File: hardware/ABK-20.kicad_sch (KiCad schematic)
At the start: 46 parts, among them J1 CONN_01X04, J2 CONN_01X04, J3 CONN_02X03, J4 Con_3-5V, J5 USB_OTG, J6 Sync_Jumper, SW1 SW_Push, SW2 SW_Push, SW3 SW_SPDT_MSM, SW4 SW_Push, U1 ATTINY85-20SU, U2 PAM8002, U3 7805

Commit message: Optimize PAM8002 audio amplifier circuit: set R14=22k for unity gain, C5=1uF, and add C8 100nF decoupling
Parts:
- added C8: 100nF, 8Bitmixtape_reworked:C_1206_HandSoldering, symbol ABK-20-rescue1:C
- C5: value 10uF -> 1uF
- R14: value 330 -> 22k
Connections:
- net GND: now also C8.2
- net VCC: now also C8.1
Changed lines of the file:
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@@
 			)
 		)
-		(property "Value" "330"
+		(property "Value" "22k"
 			(at 154.94 39.37 90)
 			(effects
@@
 			)
 		)
-		(property "Value" "10uF"
+		(property "Value" "1uF"
 			(at 137.16 40.005 0)
 			(effects
@@
 	)
 	(embedded_fonts no)
+	(junction
+		(at 107.95 24.13)
+		(diameter 0)
+		(color 0 0 0 0)
+	)
+	(junction
+		(at 107.95 36.83)
+		(diameter 0)
+		(color 0 0 0 0)
+	)
+	(wire
+		(pts
+			(xy 107.95 24.13) (xy 116.84 24.13)
+		)
+		(stroke
+			(width 0)
+			(type default)
+		)
+	)
+	(wire
+		(pts
+			(xy 116.84 24.13) (xy 116.84 26.67)
+		)
+		(stroke
+			(width 0)
+			(type default)
+		)
+	)
+	(wire
+		(pts
+			(xy 116.84 34.29) (xy 116.84 36.83)
+		)
+		(stroke
+			(width 0)
+			(type default)
+		)
+	)
+	(wire
+		(pts
+			(xy 116.84 36.83) (xy 107.95 36.83)
+		)
+		(stroke
+			(width 0)
+			(type default)
+		)
+	)
+	(symbol
+		(lib_name "C_11")
+		(lib_id "ABK-20-rescue1:C")
+		(at 116.84 30.48 0)
+		(unit 1)
+		(exclude_from_sim no)
+		(in_bom yes)
+		(on_board yes)
+		(dnp no)
+		(property "Reference" "C8"
+			(at 117.475 27.94 0)
+			(effects
+				(font
+					(size 1.27 1.27)
+				)
+				(justify left)
+			)
+		)
+		(property "Value" "100nF"
+			(at 117.475 33.02 0)
+			(effects
+				(font
+					(size 1.27 1.27)
+				)
+				(justify left)
+			)
+		)
+		(property "Footprint" "8Bitmixtape_reworked:C_1206_HandSoldering"
+			(at 117.8052 34.29 0)
+			(effects
+				(font
+					(size 1.27 1.27)
+				)
+				(hide yes)
+			)
+		)
+		(property "Datasheet" ""
+			(at 116.84 30.48 0)
+			(effects
+				(font
+					(size 1.27 1.27)
+				)
+				(hide yes)
+			)
+		)
+		(property "Description" ""
+			(at 116.84 30.48 0)
+			(effects
+				(font
+					(size 1.27 1.27)
+				)
+			)
+		)
+		(pin "1"
+		)
+		(pin "2"
+		)
+		(instances
+			(project "ABK-20"
+				(path "/586acb5e-8acc-4ed8-b81f-7b15963d193b"
+					(reference "C8")
+					(unit 1)
+				)
+			)
+		)
+	)
 )

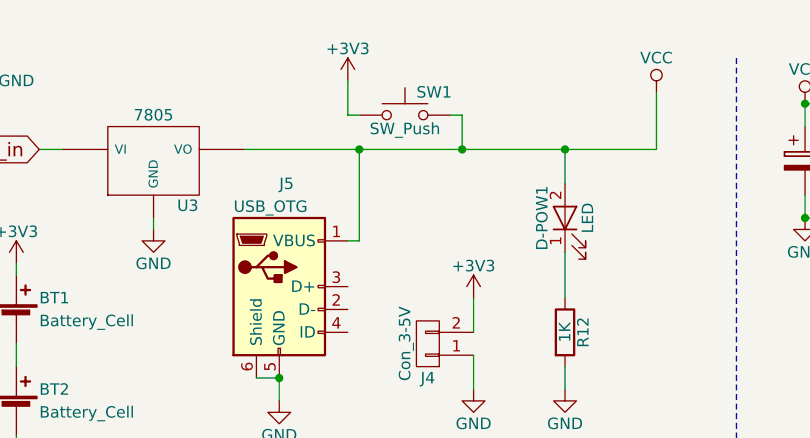
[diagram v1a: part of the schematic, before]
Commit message: Implement diode OR-ing power architecture with Schottky isolation and master latching switch
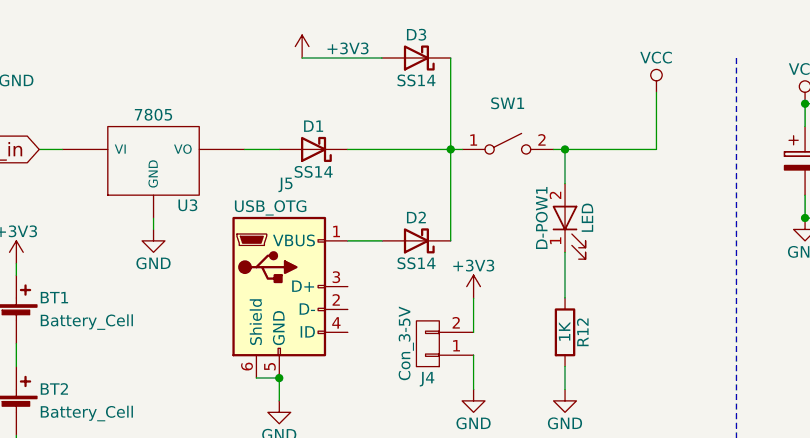
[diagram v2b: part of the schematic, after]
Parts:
- removed SW1: SW_Push, 8Bitmixtape_reworked:Push_SWITCH_hole, symbol mixtape_schematics:SW_Push
- added D1, D2, D3: SS14, Diode_SMD:D_SMA, symbol mixtape_schematics:D_Schottky
- added SW1: SW_SPST, 8Bitmixtape_reworked:Push_SWITCH_hole, symbol mixtape_schematics:SW_SPST
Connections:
- net +3V3: now also D3.2 (A)
- net VCC: now also SW1.2 (B); no longer J5.1 (VBUS), U3.VO
- new net: D1.2 (A), U3.VO
- new net: D2.2 (A), J5.1 (VBUS)
- new net: D1.1 (K), D2.1 (K), D3.1 (K), SW1.1 (A)
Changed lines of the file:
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@@
 		(color 0 0 0 0)
 	)
-	(junction
-		(at 58.42 29.21)
-		(diameter 0)
-		(color 0 0 0 0)
-	)
-	(junction
+		(junction
 		(at 140.97 111.76)
 		(diameter 0)
@@
 		(color 0 0 0 0)
 	)
-	(junction
-		(at 69.85 29.21)
-		(diameter 0)
-		(color 0 0 0 0)
-	)
-	(wire
+		(wire
 		(pts
 			(xy 248.92 152.4) (xy 242.57 152.4)
@@
 		)
 	)
-	(wire
-		(pts
-			(xy 45.72 29.21) (xy 58.42 29.21)
-		)
-		(stroke
-			(width 0)
-			(type default)
-		)
-	)
-	(wire
+		(wire
 		(pts
 			(xy 217.17 129.54) (xy 222.25 129.54)
@@
 		)
 	)
-	(wire
-		(pts
-			(xy 58.42 39.37) (xy 58.42 29.21)
-		)
-		(stroke
-			(width 0)
-			(type default)
-		)
-	)
-	(wire
+		(wire
 		(pts
 			(xy 199.39 92.71) (xy 248.92 92.71)
@@
 		)
 	)
-	(wire
-		(pts
-			(xy 57.15 25.4) (xy 58.42 25.4)
-		)
-		(stroke
-			(width 0)
-			(type default)
-		)
-	)
-	(wire
+		(wire
 		(pts
 			(xy 246.38 157.48) (xy 246.38 160.02)
@@
 		)
 	)
-	(wire
-		(pts
-			(xy 69.85 29.21) (xy 81.28 29.21)
-		)
-		(stroke
-			(width 0)
-			(type default)
-		)
-	)
-	(wire
+		(wire
 		(pts
 			(xy 161.29 39.37) (xy 165.1 39.37)
@@
 		)
 	)
-	(wire
-		(pts
-			(xy 58.42 29.21) (xy 69.85 29.21)
-		)
-		(stroke
-			(width 0)
-			(type default)
-		)
-	)
-	(wire
+		(wire
 		(pts
 			(xy 71.12 137.16) (xy 71.12 142.24)
@@
 		)
 	)
-	(wire
-		(pts
-			(xy 69.85 25.4) (xy 69.85 29.21)
-		)
-		(stroke
-			(width 0)
-			(type default)
-		)
-	)
-	(wire
+		(wire
 		(pts
 			(xy 177.8 24.13) (xy 177.8 34.29)
@@
 		)
 	)
-	(wire
-		(pts
-			(xy 57.15 21.59) (xy 57.15 25.4)
-		)
-		(stroke
-			(width 0)
-			(type default)
-		)
-	)
-	(wire
+		(wire
 		(pts
 			(xy 71.12 52.07) (xy 71.12 55.88)
@@
 		)
 	)
-	(wire
-		(pts
-			(xy 57.15 39.37) (xy 58.42 39.37)
-		)
-		(stroke
-			(width 0)
-			(type default)
-		)
-	)
-	(wire
+		(wire
 		(pts
 			(xy 182.88 104.14) (xy 182.88 106.68)
@@
 		)
 	)
-	(wire
-		(pts
-			(xy 68.58 25.4) (xy 69.85 25.4)
-		)
-		(stroke
-			(width 0)
-			(type default)
-		)
-	)
-	(wire
+		(wire
 		(pts
 			(xy 144.78 93.98) (xy 152.4 93.98)
@@
 		)
 	)
-	(symbol
-		(lib_id "mixtape_schematics:SW_Push")
-		(at 63.5 25.4 0)
-		(unit 1)
-		(exclude_from_sim no)
-		(in_bom yes)
-		(on_board yes)
-		(dnp no)
-		(property "Reference" "SW1"
-			(at 64.77 22.86 0)
-			(effects
-				(font
-					(size 1.27 1.27)
-				)
-				(justify left)
-			)
-		)
-		(property "Value" "SW_Push"
-			(at 63.5 26.924 0)
-			(effects
-				(font
-					(size 1.27 1.27)
-				)
-			)
-		)
-		(property "Footprint" "8Bitmixtape_reworked:Push_SWITCH_hole"
-			(at 63.5 20.32 0)
-			(effects
-				(font
-					(size 1.27 1.27)
-				)
-				(hide yes)
-			)
-		)
-		(property "Datasheet" ""
-			(at 63.5 20.32 0)
-			(effects
-				(font
-					(size 1.27 1.27)
-				)
-				(hide yes)
-			)
-		)
-		(property "Description" ""
-			(at 63.5 25.4 0)
-			(effects
-				(font
-					(size 1.27 1.27)
-				)
-			)
-		)
-		(pin "1"
-		)
-		(pin "2"
-		)
-		(instances
-			(project "ABK-20"
-				(path "/586acb5e-8acc-4ed8-b81f-7b15963d193b"
-					(reference "SW1")
-					(unit 1)
-				)
-			)
-		)
-	)
-	(symbol
+		(symbol
 		(lib_id "mixtape_schematics:SW_Push")
 		(at 111.76 161.29 270)
@@
 		(lib_name "+3V3_6")
 		(lib_id "ABK-20-rescue1:+3V3")
-		(at 57.15 21.59 0)
+		(at 52.07 19.05 0)
 		(unit 1)
 		(exclude_from_sim no)
@@
 		(dnp no)
 		(property "Reference" "#PWR026"
-			(at 57.15 25.4 0)
+			(at 52.07 22.86 0)
 			(effects
 				(font
@@
 		)
 		(property "Footprint" ""
-			(at 57.15 21.59 0)
+			(at 52.07 19.05 0)
 			(effects
 				(font
@@
 		)
 		(property "Datasheet" ""
-			(at 57.15 21.59 0)
+			(at 52.07 19.05 0)
 			(effects
 				(font
@@
 		)
 		(property "Description" ""
-			(at 57.15 21.59 0)
+			(at 52.07 19.05 0)
 			(effects
 				(font
@@
 			)
 		)
+	)
+	(junction
+		(at 68.58 29.21)
+		(diameter 0)
+		(color 0 0 0 0)
+	)
+	(wire
+		(pts
+			(xy 45.72 29.21) (xy 49.53 29.21)
+		)
+		(stroke (width 0) (type default))
+	)
+	(wire
+		(pts
+			(xy 57.15 29.21) (xy 68.58 29.21)
+		)
+		(stroke (width 0) (type default))
+	)
+	(wire
+		(pts
+			(xy 57.15 39.37) (xy 60.96 39.37)
+		)
+		(stroke (width 0) (type default))
+	)
+	(wire
+		(pts
+			(xy 68.58 39.37) (xy 68.58 29.21)
+		)
+		(stroke (width 0) (type default))
+	)
+	(wire
+		(pts
+			(xy 52.07 19.05) (xy 60.96 19.05)
+		)
+		(stroke (width 0) (type default))
+	)
+	(wire
+		(pts
+			(xy 68.58 19.05) (xy 68.58 29.21)
+		)
+		(stroke (width 0) (type default))
+	)
+	(wire
+		(pts
+			(xy 68.58 29.21) (xy 69.85 29.21)
+		)
+		(stroke (width 0) (type default))
+	)
+	(wire
+		(pts
+			(xy 80.01 29.21) (xy 81.28 29.21)
+		)
+		(stroke (width 0) (type default))
+	)
+	(symbol
+		(lib_id "mixtape_schematics:D_Schottky")
+		(at 53.34 29.21 180)
+		(unit 1)
+		(exclude_from_sim no)
+		(in_bom yes)
+		(on_board yes)
+		(dnp no)
+		(property "Reference" "D1"
+			(at 53.34 26.67 0)
+			(effects (font (size 1.27 1.27)))
+		)
+		(property "Value" "SS14"
+			(at 53.34 31.75 0)
+			(effects (font (size 1.27 1.27)))
+		)
+		(property "Footprint" "Diode_SMD:D_SMA"
+			(at 53.34 29.21 0)
+			(effects (font (size 1.27 1.27)) (hide yes))
+		)
+		(property "Datasheet" "~"
+			(at 53.34 29.21 0)
+			(effects (font (size 1.27 1.27)) (hide yes))
+		)
+		(property "Description" "Schottky Diode (7805 DC In Protection)"
+			(at 53.34 29.21 0)
+			(effects (font (size 1.27 1.27)) (hide yes))
+		)
+		(pin "1")
+		(pin "2")
+		(instances
+			(project "ABK-20"
+				(path "/586acb5e-8acc-4ed8-b81f-7b15963d193b" (reference "D1") (unit 1))
+			)
+		)
+	)
+	(symbol
+		(lib_id "mixtape_schematics:D_Schottky")
+		(at 64.77 39.37 180)
+		(unit 1)
+		(exclude_from_sim no)
+		(in_bom yes)
+		(on_board yes)
+		(dnp no)
+		(property "Reference" "D2"
+			(at 64.77 36.83 0)
+			(effects (font (size 1.27 1.27)))
+		)
+		(property "Value" "SS14"
+			(at 64.77 41.91 0)
+			(effects (font (size 1.27 1.27)))
+		)
+		(property "Footprint" "Diode_SMD:D_SMA"
+			(at 64.77 39.37 0)
+			(effects (font (size 1.27 1.27)) (hide yes))
+		)
+		(property "Datasheet" "~"
+			(at 64.77 39.37 0)
+			(effects (font (size 1.27 1.27)) (hide yes))
+		)
+		(property "Description" "Schottky Diode (USB VBUS Protection)"
+			(at 64.77 39.37 0)
+			(effects (font (size 1.27 1.27)) (hide yes))
+		)
+		(pin "1")
+		(pin "2")
+		(instances
+			(project "ABK-20"
+				(path "/586acb5e-8acc-4ed8-b81f-7b15963d193b" (reference "D2") (unit 1))
+			)
+		)
+	)
+	(symbol
+		(lib_id "mixtape_schematics:D_Schottky")
+		(at 64.77 19.05 180)
+		(unit 1)
+		(exclude_from_sim no)
+		(in_bom yes)
+		(on_board yes)
+		(dnp no)
+		(property "Reference" "D3"
+			(at 64.77 16.51 0)
+			(effects (font (size 1.27 1.27)))
+		)
+		(property "Value" "SS14"
+			(at 64.77 21.59 0)
+			(effects (font (size 1.27 1.27)))
+		)
+		(property "Footprint" "Diode_SMD:D_SMA"
+			(at 64.77 19.05 0)
+			(effects (font (size 1.27 1.27)) (hide yes))
+		)
+		(property "Datasheet" "~"
+			(at 64.77 19.05 0)
+			(effects (font (size 1.27 1.27)) (hide yes))
+		)
+		(property "Description" "Schottky Diode (Battery Reverse Protection)"
+			(at 64.77 19.05 0)
+			(effects (font (size 1.27 1.27)) (hide yes))
+		)
+		(pin "1")
+		(pin "2")
+		(instances
+			(project "ABK-20"
+				(path "/586acb5e-8acc-4ed8-b81f-7b15963d193b" (reference "D3") (unit 1))
+			)
+		)
+	)
+	(symbol
+		(lib_id "mixtape_schematics:SW_SPST")
+		(at 74.93 29.21 0)
+		(unit 1)
+		(exclude_from_sim no)
+		(in_bom yes)
+		(on_board yes)
+		(dnp no)
+		(property "Reference" "SW1"
+			(at 74.93 24.13 0)
+			(effects (font (size 1.27 1.27)))
+		)
+		(property "Value" "SW_SPST"
+			(at 74.93 34.29 0)
+			(effects (font (size 1.27 1.27)) (hide yes))
+		)
+		(property "Footprint" "8Bitmixtape_reworked:Push_SWITCH_hole"
+			(at 74.93 29.21 0)
+			(effects (font (size 1.27 1.27)) (hide yes))
+		)
+		(property "Datasheet" ""
+			(at 74.93 29.21 0)
+			(effects (font (size 1.27 1.27)) (hide yes))
+		)
+		(property "Description" "Master Latching Power Switch"
+			(at 74.93 29.21 0)
+			(effects (font (size 1.27 1.27)) (hide yes))
+		)
+		(pin "1")
+		(pin "2")
+		(instances
+			(project "ABK-20"
+				(path "/586acb5e-8acc-4ed8-b81f-7b15963d193b" (reference "SW1") (unit 1))
+			)
+		)

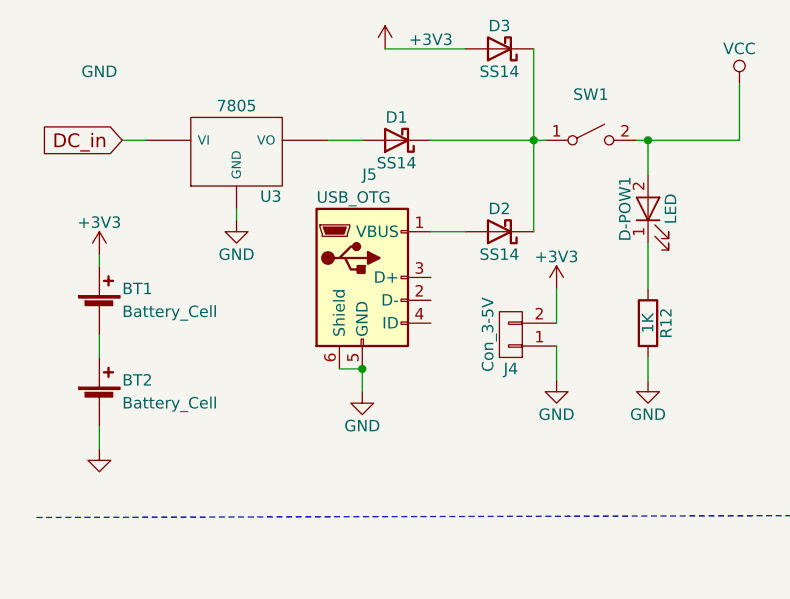
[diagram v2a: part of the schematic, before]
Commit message: Replace USB connector with 6-pin USB-C power-only receptacle symbol (J5)
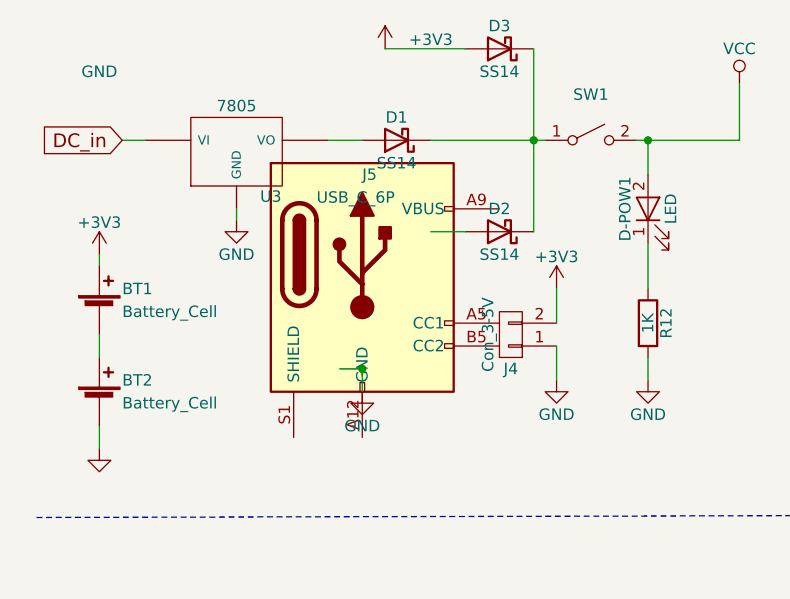
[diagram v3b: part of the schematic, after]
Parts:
- J5: value USB_OTG -> USB_C_6P; footprint 8Bitmixtape_reworked:USB_Micro-B -> 8Bitmixtape_reworked:USB_C_6Pin_PowerOnly; symbol ABK-20-rescue1:USB_OTG -> mixtape_schematics:USB_C_Receptacle_PowerOnly_6P
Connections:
- net GND: no longer J5.5 (GND), J5.6 (Shield)
- net at D2.2 (A): no longer J5.1 (VBUS)
- new net: J5.A12 (GND), J5.B12 (GND)
- new net: J5.A9 (VBUS), J5.B9 (VBUS)
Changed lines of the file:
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@@
 	)
 	(symbol
-		(lib_name "USB_OTG_2")
-		(lib_id "ABK-20-rescue1:USB_OTG")
+		(lib_id "mixtape_schematics:USB_C_Receptacle_PowerOnly_6P")
 		(at 49.53 44.45 0)
 		(unit 1)
@@
 			)
 		)
-		(property "Value" "USB_OTG"
+		(property "Value" "USB_C_6P"
 			(at 44.45 35.56 0)
 			(effects
@@
 			)
 		)
-		(property "Footprint" "8Bitmixtape_reworked:USB_Micro-B"
-			(at 53.34 45.72 0)
+		(property "Footprint" "8Bitmixtape_reworked:USB_C_6Pin_PowerOnly"
+			(at 49.53 44.45 0)
 			(effects
 				(font
@@
 			)
 		)
-		(property "Datasheet" ""
-			(at 53.34 45.72 0)
+		(property "Datasheet" "https://www.usb.org/sites/default/files/documents/usb_type-c.zip"
+			(at 49.53 44.45 0)
 			(effects
 				(font
@@
 			)
 		)
-		(property "Description" ""
+		(property "Description" "USB Power-Only 6P Type-C Receptacle connector"
 			(at 49.53 44.45 0)
 			(effects
@@
 					(size 1.27 1.27)
 				)
+				(hide yes)
 			)
 		)
-		(pin "6"
+		(pin "A12"
 		)
-		(pin "5"
+		(pin "A5"
 		)
-		(pin "1"
+		(pin "A9"
 		)
-		(pin "3"
+		(pin "B12"
 		)
-		(pin "2"
+		(pin "B5"
 		)
-		(pin "4"
+		(pin "B9"
+		)
+		(pin "S1"
+			(uuid "s1000000-0000-4000-8000-000000000007")
 		)
 		(instances

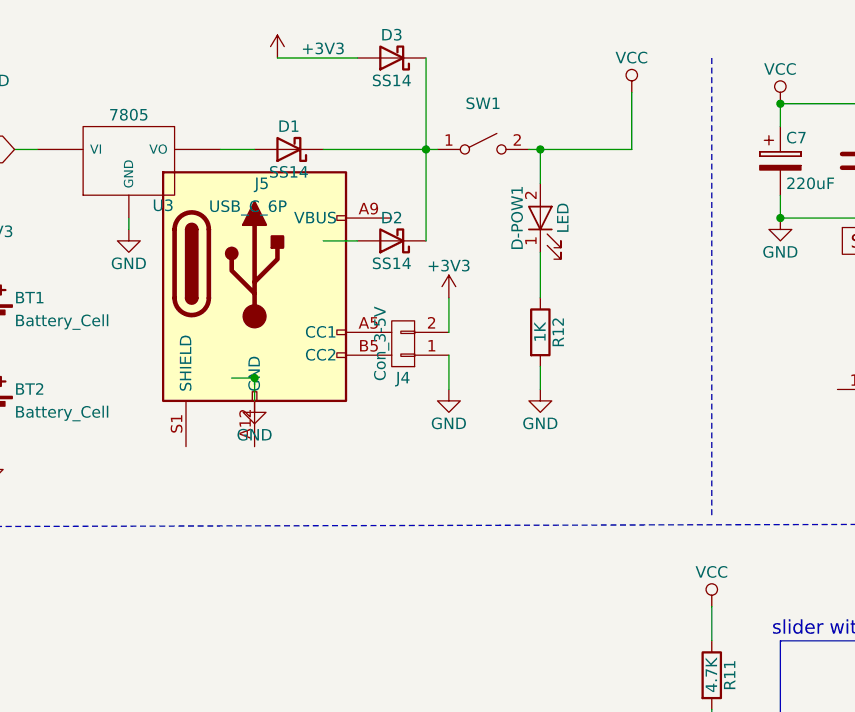
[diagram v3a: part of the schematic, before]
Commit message: Add 5.1k pull-down resistors (R17, R18) on USB-C CC1 and CC2 for USB-PD detection
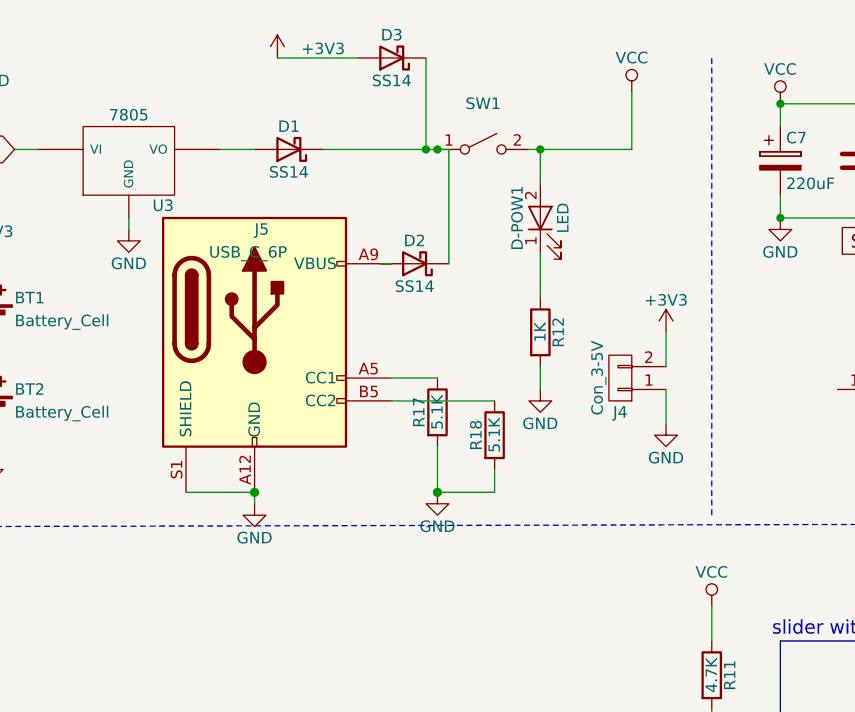
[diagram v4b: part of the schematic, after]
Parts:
- added R17, R18: 5.1K, 8Bitmixtape_reworked:R_0805_HandSoldering, symbol ABK-20-rescue1:R
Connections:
- net GND: now also J5.A12 (GND), J5.B12 (GND), J5.S1 (SHIELD), R17.2, R18.2
- net at J5.A5 (CC1): now also R17.1
- net at J5.A9 (VBUS), J5.B9 (VBUS): now also D2.2 (A)
- net at J5.B5 (CC2): now also R18.1
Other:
- moved on the sheet: D2, J4, J5

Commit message: Allocate footprints for all components: RV1 (PTL20), SW3 (SPDT), R17/R18 (1206), U3 (TO-252)
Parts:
- R17, R18: footprint 8Bitmixtape_reworked:R_0805_HandSoldering -> 8Bitmixtape_reworked:R_1206_HandSoldering
- RV1: footprint (none) -> 8Bitmixtape_reworked:Potentiometer_Bourns_PTL20_Single_Slide_LED
- SW3: footprint (none) -> 8Bitmixtape_reworked:SWITCH-SPDT_KIT
- U3: footprint TO_SOT_Packages_SMD:TO-252-3_TabPin2 -> Package_TO_SOT_SMD:TO-252-3_TabPin2
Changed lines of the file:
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@@
 			)
 		)
-		(property "Footprint" "TO_SOT_Packages_SMD:TO-252-3_TabPin2"
+		(property "Footprint" "Package_TO_SOT_SMD:TO-252-3_TabPin2"
 			(at 35.56 30.48 0)
 			(effects
@@
 			)
 		)
-		(property "Footprint" "8Bitmixtape_reworked:R_0805_HandSoldering"
+		(property "Footprint" "8Bitmixtape_reworked:R_1206_HandSoldering"
 			(at 71.628 58.42 90)
 			(effects
@@
 			)
 		)
-		(property "Footprint" "8Bitmixtape_reworked:R_0805_HandSoldering"
+		(property "Footprint" "8Bitmixtape_reworked:R_1206_HandSoldering"
 			(at 77.978 60.96 90)
 			(effects
@@
 			)
 		)
-		(property "Footprint" ""
+		(property "Footprint" "8Bitmixtape_reworked:SWITCH-SPDT_KIT"
 			(at 76.2 175.26 0)
 			(effects
@@
 			)
 		)
-		(property "Footprint" ""
+		(property "Footprint" "8Bitmixtape_reworked:Potentiometer_Bourns_PTL20_Single_Slide_LED"
 			(at 124.46 88.9 0)
 			(effects
@@
 			)
 		)
-		(property "Footprint" ""
+		(property "Footprint" "8Bitmixtape_reworked:Potentiometer_Bourns_PTL20_Single_Slide_LED"
 			(at 114.3 101.6 0)
 			(effects

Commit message: feat(footprint): update slide pot to Bourns PTL30 (30mm travel, +-20mm column pitch)
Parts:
- RV1: footprint 8Bitmixtape_reworked:Potentiometer_Bourns_PTL20_Single_Slide_LED -> 8Bitmixtape_reworked:Potentiometer_Bourns_PTL30_Single_Slide_LED
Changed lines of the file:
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@@
 			)
 		)
-		(property "Footprint" "8Bitmixtape_reworked:Potentiometer_Bourns_PTL20_Single_Slide_LED"
+		(property "Footprint" "8Bitmixtape_reworked:Potentiometer_Bourns_PTL30_Single_Slide_LED"
 			(at 124.46 88.9 0)
 			(effects
@@
 			)
 		)
-		(property "Footprint" "8Bitmixtape_reworked:Potentiometer_Bourns_PTL20_Single_Slide_LED"
+		(property "Footprint" "8Bitmixtape_reworked:Potentiometer_Bourns_PTL30_Single_Slide_LED"
 			(at 114.3 101.6 0)
 			(effects
